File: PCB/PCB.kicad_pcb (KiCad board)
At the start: 2 copper layers, 116 x 41 mm, 38 parts, among them J1 sw, J2 sw, J3 detectors, J4 IR, SW1 SW_SPST, SW2 SW_SPST, SW3 SW_SPST, SW4 SW_SPST, U2 PC827, U3 24LC512, U4 24LC512, U5 24LC512, U6 24LC512

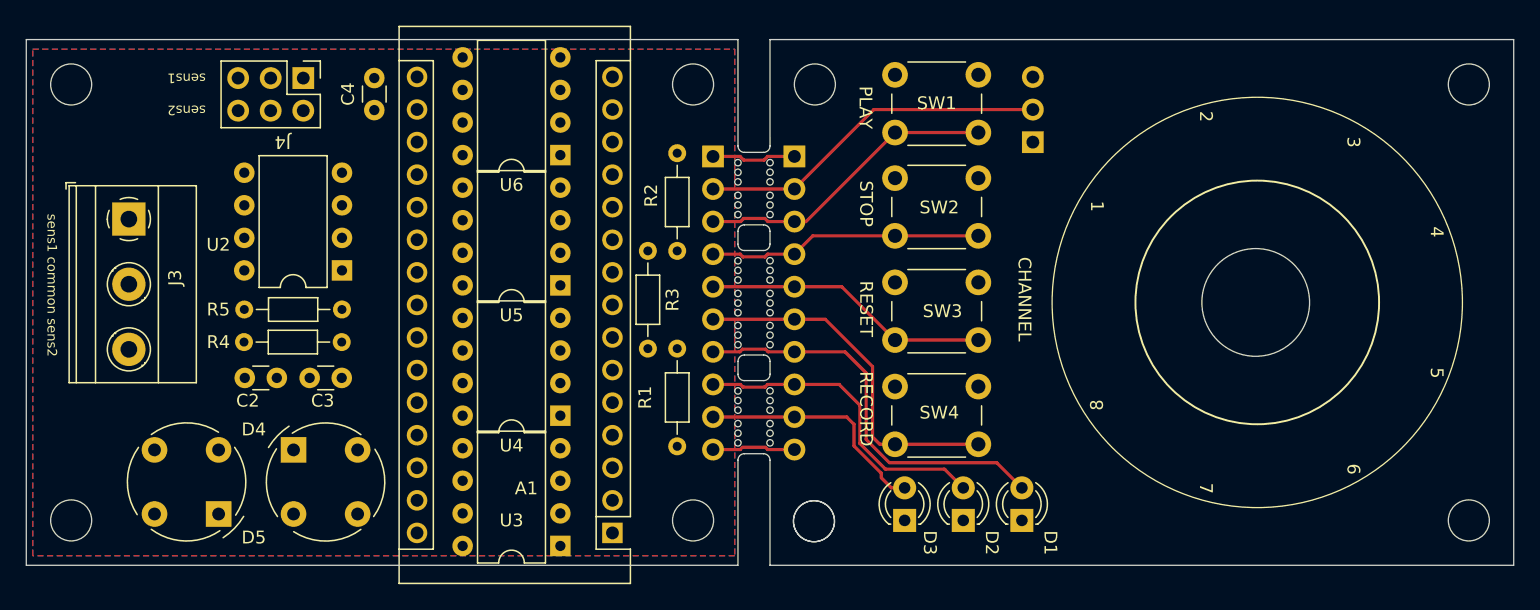
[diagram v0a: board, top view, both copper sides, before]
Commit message: did routing of PCB design. I must investigate if I want an extra I2C port to be used with I2C to create extra buttons to this system
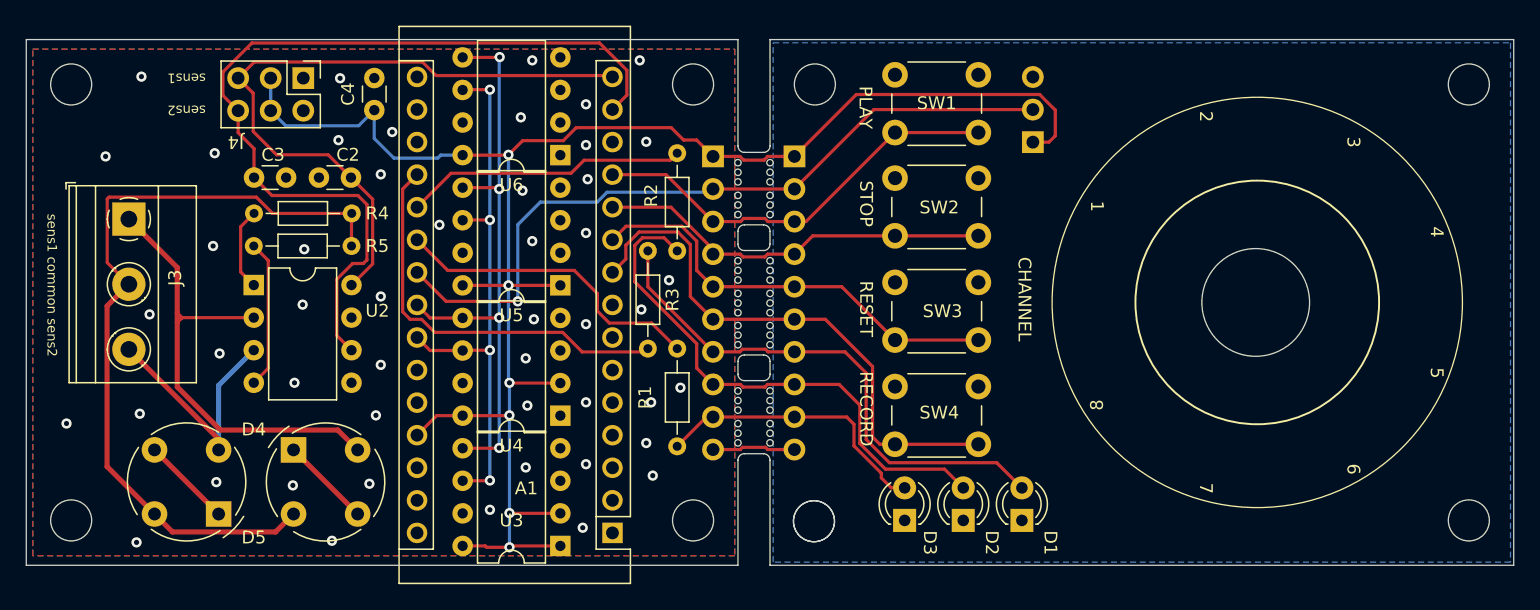
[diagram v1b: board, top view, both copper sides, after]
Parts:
- moved C2 17.7 mm to (102.3, 88.3), turned to 180 degrees
- moved C3 17.1 mm to (94.8, 88.3), turned to 0 degrees
- moved R4 13.1 mm to (102.4, 91.1), turned to 180 degrees
- moved R5 8.47 mm to (94.7, 93.6), turned to 0 degrees
- moved U2 6.97 mm to (94.7, 96.6), turned to 0 degrees
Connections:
- A1 pad 10: /stop -> /reset
- A1 pad 11: /play -> /stop
- A1 pad 12: /reset -> /play
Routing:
- net +5V: track 6.59 -> 138.0 mm, vias 0 -> 6
- net /sensor2: track 0.00 -> 69.1 mm
- net Net-(D4-Pad2): track 0.00 -> 61.7 mm
- net /sensor1: track 0.00 -> 53.7 mm
- net /SDA: track 0.00 -> 46.0 mm, vias 0 -> 4
- net /SCL: track 0.00 -> 43.0 mm, vias 0 -> 4
- net Net-(D4-Pad4): track 0.00 -> 37.4 mm
- net Net-(A1-Pad19): track 0.00 -> 31.7 mm
- net /channel: track 27.5 -> 58.7 mm, vias 0 -> 1
- net Net-(A1-Pad21): track 0.00 -> 24.6 mm
- net Net-(A1-Pad20): track 0.00 -> 22.0 mm
- net Net-(D5-Pad2): track 0.00 -> 19.7 mm
- net /yellow: track 24.8 -> 42.1 mm
- net /record: track 28.0 -> 42.9 mm
- net Net-(R5-Pad1): track 0.00 -> 11.6 mm
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
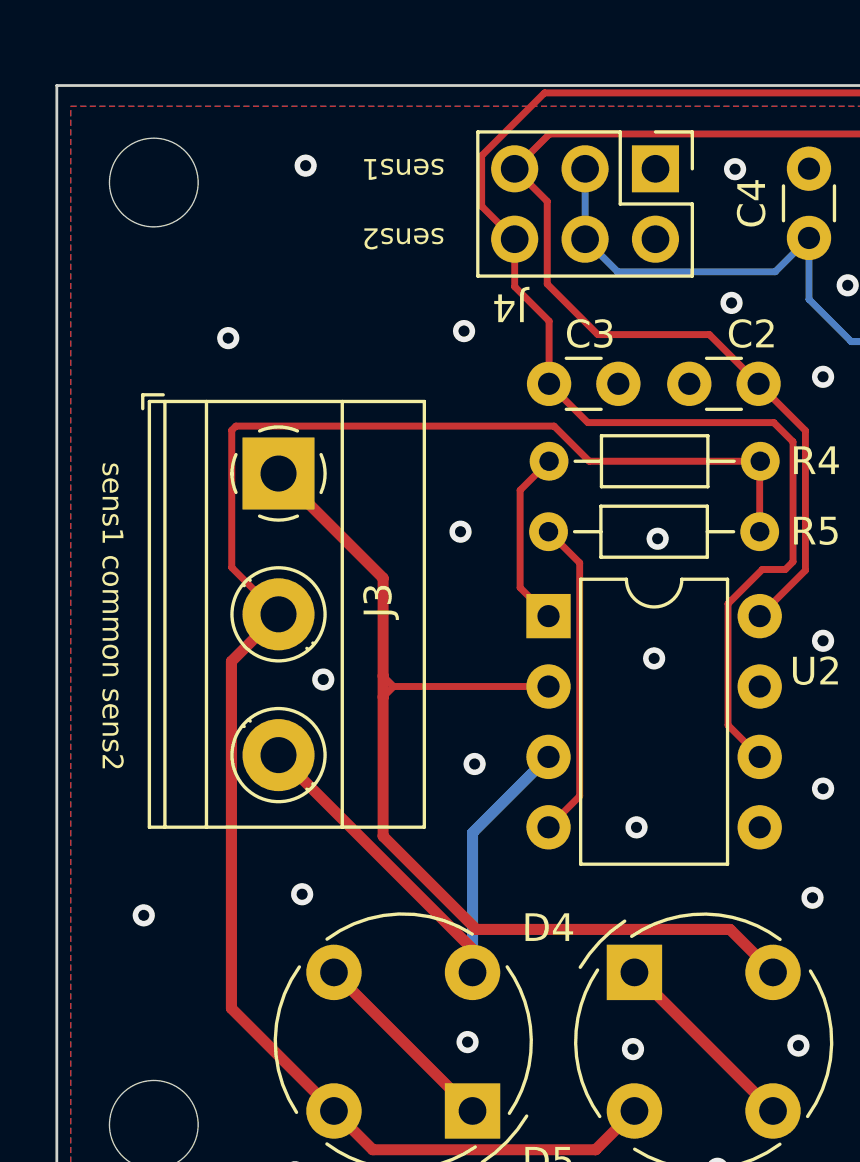
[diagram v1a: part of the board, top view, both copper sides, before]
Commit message: added I2C connector on the side. Routing needs to be re done for a large part
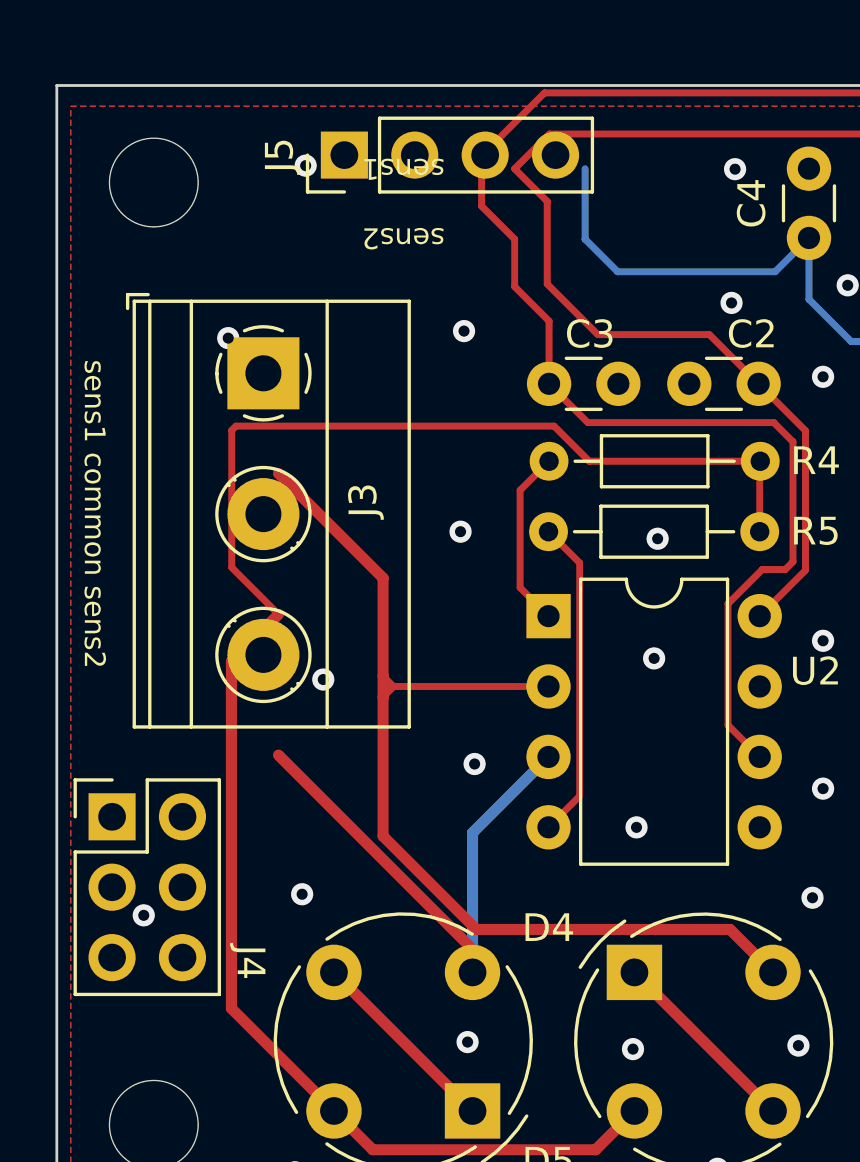
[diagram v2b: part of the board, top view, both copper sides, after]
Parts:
- added J5: I2C, Connector_PinHeader_2.54mm:PinHeader_1x04_P2.54mm_Vertical, F.Cu at (87.4, 80.0)
- moved J4 30.5 mm to (79.0, 103.9), turned to 0 degrees
- moved J3 3.66 mm to (84.5, 87.9)
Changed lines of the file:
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@@
   (net 43 "Net-(A1-Pad21)")
   (footprint "TerminalBlock_Phoenix:TerminalBlock_Phoenix_MKDS-1,5-3-5.08_1x03_P5.08mm_Horizontal" (layer "F.Cu")
-    (at 85 91.5 -90)
+    (at 84.455 87.884 -90)
     (descr "Terminal Block Phoenix MKDS-1,5-3-5.08, 3 pins, pitch 5.08mm, size 15.2x9.8mm^2, drill diamater 1.3mm, pad diameter 2.6mm, see http://www.farnell.com/datasheets/100425.pdf, script-generated using https://github.com/pointhi/kicad-footprint-generator/scripts/TerminalBlock_Phoenix")
     (tags "THT Terminal Block Phoenix MKDS-1,5-3-5.08 pitch 5.08mm size 15.2x9.8mm^2 drill 1.3mm pad 2.6mm")
@@
     )
   )
+  (footprint "Connector_PinHeader_2.54mm:PinHeader_1x04_P2.54mm_Vertical" (layer "F.Cu")
+    (at 87.376 80.01 90)
+    (descr "Through hole straight pin header, 1x04, 2.54mm pitch, single row")
+    (tags "Through hole pin header THT 1x04 2.54mm single row")
+    (property "Sheetfile" "PCB.kicad_sch")
+    (property "Sheetname" "")
+    (attr through_hole)
+    (fp_text reference "J5" (at 0 -2.33 90) (layer "F.SilkS")
+      (effects (font (size 1 1) (thickness 0.15)))
+    )
+    (fp_text value "I2C" (at 0 9.95 90) (layer "F.Fab")
+      (effects (font (size 1 1) (thickness 0.15)))
+    )
+    (fp_text user "${REFERENCE}" (at 0 3.81) (layer "F.Fab")
+      (effects (font (size 1 1) (thickness 0.15)))
+    )
+    (fp_line (start -1.33 1.27) (end -1.33 8.95) (layer "F.SilkS") (width 0.12))
+    (fp_line (start -1.33 1.27) (end 1.33 1.27) (layer "F.SilkS") (width 0.12))
+    (fp_line (start -1.33 -1.33) (end 0 -1.33) (layer "F.SilkS") (width 0.12))
+    (fp_line (start -1.33 8.95) (end 1.33 8.95) (layer "F.SilkS") (width 0.12))
+    (fp_line (start 1.33 1.27) (end 1.33 8.95) (layer "F.SilkS") (width 0.12))
+    (fp_line (start -1.33 0) (end -1.33 -1.33) (layer "F.SilkS") (width 0.12))
+    (fp_line (start -1.8 9.4) (end 1.8 9.4) (layer "F.CrtYd") (width 0.05))
+    (fp_line (start -1.8 -1.8) (end -1.8 9.4) (layer "F.CrtYd") (width 0.05))
+    (fp_line (start 1.8 -1.8) (end -1.8 -1.8) (layer "F.CrtYd") (width 0.05))
+    (fp_line (start 1.8 9.4) (end 1.8 -1.8) (layer "F.CrtYd") (width 0.05))
+    (fp_line (start -1.27 8.89) (end -1.27 -0.635) (layer "F.Fab") (width 0.1))
+    (fp_line (start -1.27 -0.635) (end -0.635 -1.27) (layer "F.Fab") (width 0.1))
+    (fp_line (start 1.27 -1.27) (end 1.27 8.89) (layer "F.Fab") (width 0.1))
+    (fp_line (start 1.27 8.89) (end -1.27 8.89) (layer "F.Fab") (width 0.1))
+    (fp_line (start -0.635 -1.27) (end 1.27 -1.27) (layer "F.Fab") (width 0.1))
+    (pad "1" thru_hole rect locked (at 0 0 90) (size 1.7 1.7) (drill 1) (layers *.Cu *.Mask)
+      (net 19 "/SCL") (pinfunction "Pin_1") (pintype "passive"))
+    (pad "2" thru_hole oval locked (at 0 2.54 90) (size 1.7 1.7) (drill 1) (layers *.Cu *.Mask)
+      (net 18 "/SDA") (pinfunction "Pin_2") (pintype "passive"))
+    (pad "3" thru_hole oval locked (at 0 5.08 90) (size 1.7 1.7) (drill 1) (layers *.Cu *.Mask)
+      (net 22 "+5V") (pinfunction "Pin_3") (pintype "passive"))
+    (pad "4" thru_hole oval locked (at 0 7.62 90) (size 1.7 1.7) (drill 1) (layers *.Cu *.Mask)
+      (net 4 "GND") (pinfunction "Pin_4") (pintype "passive"))
+    (model "${KICAD6_3DMODEL_DIR}/Connector_PinHeader_2.54mm.3dshapes/PinHeader_1x04_P2.54mm_Vertical.wrl"
+      (offset (xyz 0 0 0))
+      (scale (xyz 1 1 1))
+      (rotate (xyz 0 0 0))
+    )
+  )
   (footprint "Diode_THT:Diode_Bridge_Round_D9.0mm" (layer "F.Cu")
     (at 92 114.5 180)
@@
   )
   (footprint "Connector_PinHeader_2.54mm:PinHeader_2x03_P2.54mm_Vertical" (layer "F.Cu")
-    (at 98.601 80.505 -90)
+    (at 78.994 103.886)
     (descr "Through hole straight pin header, 2x03, 2.54mm pitch, double rows")
     (tags "Through hole pin header THT 2x03 2.54mm double row")
@@
     (property "Sheetname" "")
     (attr through_hole)
-    (fp_text reference "J4" (at 4.995 5.256 180 unlocked) (layer "F.SilkS")
-      (effects (font (size 1 1) (thickness 0.15)))
-    )
-    (fp_text value "IR" (at 1.27 7.41 90) (layer "F.Fab")
-      (effects (font (size 1 1) (thickness 0.15)))
-    )
-    (fp_text user "${REFERENCE}" (at 1.27 2.54) (layer "F.Fab")
+    (fp_text reference "J4" (at 4.995 5.256 270 unlocked) (layer "F.SilkS")
+      (effects (font (size 1 1) (thickness 0.15)))
+    )
+    (fp_text value "IR" (at 1.27 7.41) (layer "F.Fab")
+      (effects (font (size 1 1) (thickness 0.15)))
+    )
+    (fp_text user "${REFERENCE}" (at 1.27 2.54 90) (layer "F.Fab")
       (effects (font (size 1 1) (thickness 0.15)))
     )
@@
     (fp_line (start -1.27 0) (end 0 -1.27) (layer "F.Fab") (width 0.1))
     (fp_line (start 3.81 6.35) (end -1.27 6.35) (layer "F.Fab") (width 0.1))
-    (pad "1" thru_hole rect (at 0 0 270) (size 1.7 1.7) (drill 1) (layers *.Cu *.Mask)
+    (pad "1" thru_hole rect (at 0 0) (size 1.7 1.7) (drill 1) (layers *.Cu *.Mask)
       (net 4 "GND") (pinfunction "Pin_1") (pintype "passive"))
-    (pad "2" thru_hole oval (at 2.54 0 270) (size 1.7 1.7) (drill 1) (layers *.Cu *.Mask)
+    (pad "2" thru_hole oval (at 2.54 0) (size 1.7 1.7) (drill 1) (layers *.Cu *.Mask)
       (net 4 "GND") (pinfunction "Pin_2") (pintype "passive"))
-    (pad "3" thru_hole oval (at 0 2.54 270) (size 1.7 1.7) (drill 1) (layers *.Cu *.Mask)
+    (pad "3" thru_hole oval (at 0 2.54) (size 1.7 1.7) (drill 1) (layers *.Cu *.Mask)
       (net 22 "+5V") (pinfunction "Pin_3") (pintype "passive"))
-    (pad "4" thru_hole oval (at 2.54 2.54 270) (size 1.7 1.7) (drill 1) (layers *.Cu *.Mask)
+    (pad "4" thru_hole oval (at 2.54 2.54) (size 1.7 1.7) (drill 1) (layers *.Cu *.Mask)
       (net 22 "+5V") (pinfunction "Pin_4") (pintype "passive"))
-    (pad "5" thru_hole oval (at 0 5.08 270) (size 1.7 1.7) (drill 1) (layers *.Cu *.Mask)
+    (pad "5" thru_hole oval (at 0 5.08) (size 1.7 1.7) (drill 1) (layers *.Cu *.Mask)
       (net 11 "/sensor1") (pinfunction "Pin_5") (pintype "passive"))
-    (pad "6" thru_hole oval (at 2.54 5.08 270) (size 1.7 1.7) (drill 1) (layers *.Cu *.Mask)
+    (pad "6" thru_hole oval (at 2.54 5.08) (size 1.7 1.7) (drill 1) (layers *.Cu *.Mask)
       (net 10 "/sensor2") (pinfunction "Pin_6") (pintype "passive"))
     (model "${KICAD6_3DMODEL_DIR}/Connector_PinHeader_2.54mm.3dshapes/PinHeader_2x03_P2.54mm_Vertical.wrl"
@@
   (gr_arc (start 133 93.95) (mid 132.646437 93.803563) (end 132.5 93.45) (layer "Edge.Cuts") (width 0.1))
   (gr_line (start 133 109.8) (end 134.5 109.8) (layer "Edge.Cuts") (width 0.1))
-  (gr_text "sens1 common sens2" (at 79 96.66 270) (layer "F.SilkS")
+  (gr_text "sens1 common sens2" (at 78.359 92.964 270) (layer "F.SilkS")
     (effects (font (size 0.75 0.75) (thickness 0.15)))
   )
